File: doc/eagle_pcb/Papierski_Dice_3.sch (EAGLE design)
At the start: 17 parts

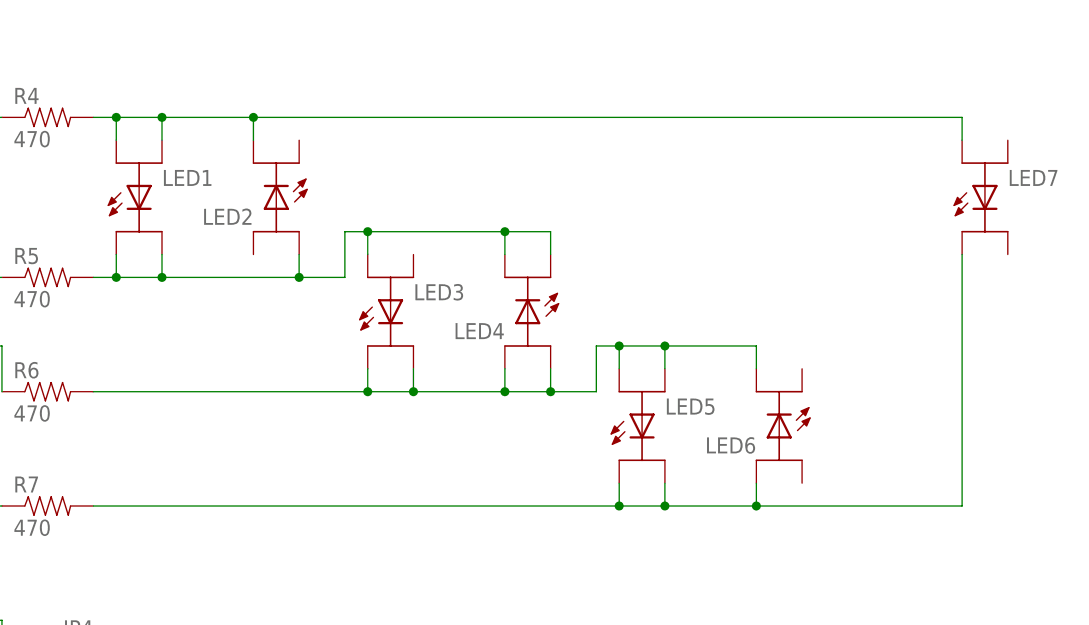
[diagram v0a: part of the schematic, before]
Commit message: Updated schematic to specify where each led was physically
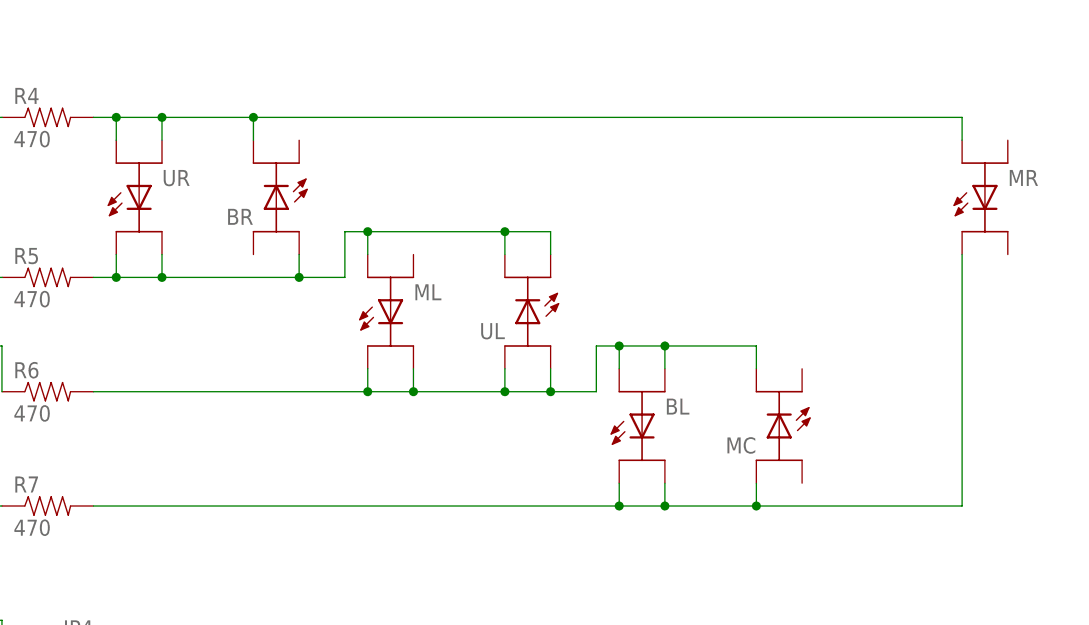
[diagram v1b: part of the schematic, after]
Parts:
- renumbered LED1 to UR, LED2 to BR, LED3 to ML, LED4 to UL, LED5 to BL, LED6 to MC, LED7 to MR
